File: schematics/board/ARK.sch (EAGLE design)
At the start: 85 parts, among them IC2 STM32F103C8T

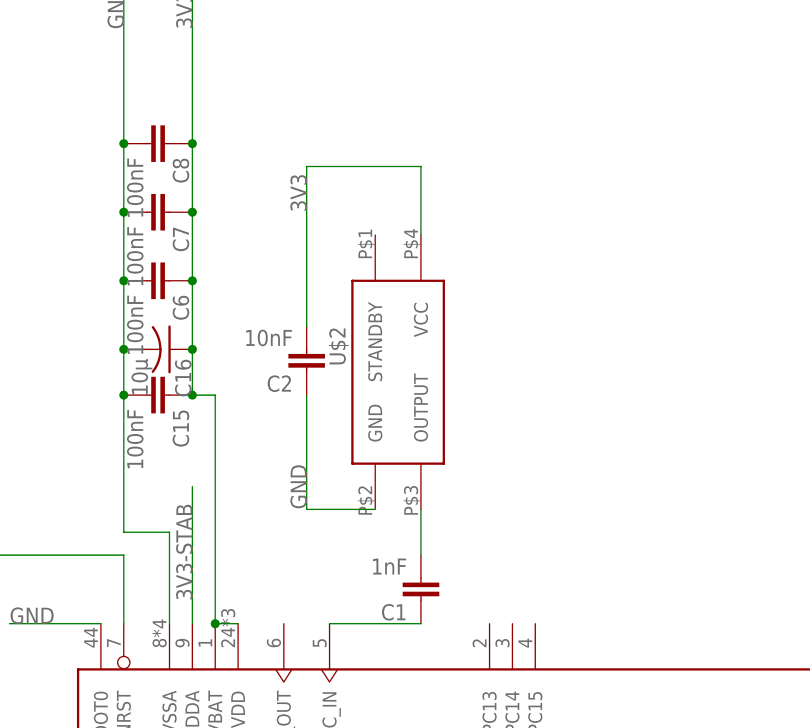
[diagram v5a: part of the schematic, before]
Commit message: Завершена разработка плат БСК5 и АРК, половина платы БКУ разведена, добавлены гербер файлы плат АРК, БСК5 и WSPR
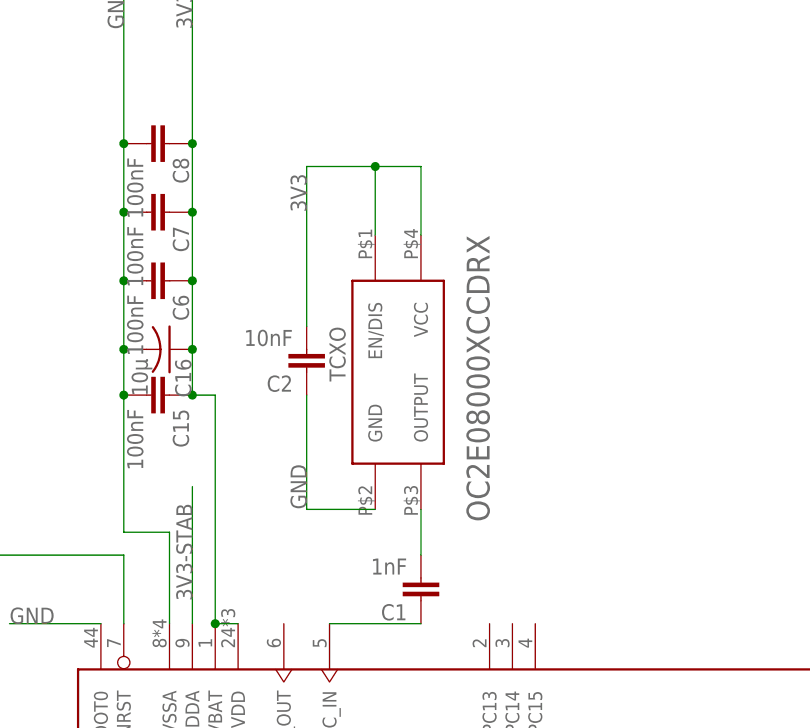
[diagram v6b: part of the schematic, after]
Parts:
- removed U$2: Q24, CanCubeSat:Q24
- added TCXO: OC2E08000XCCDRX, CanCubeSat:OC2E08000XCCDRX
- renumbered U$57 to INA219#2
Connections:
- net 3V3: now also TCXO.EN/DIS, TCXO.VCC; no longer U$2.VCC
- net GND: now also TCXO.GND; no longer U$2.GND
- net N$4: now also TCXO.OUTPUT; no longer U$2.OUTPUT
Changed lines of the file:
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@@
 <part name="R77" library="resistor" deviceset="R-US_" device="R0603" package3d_urn="urn:adsk.eagle:package:23555/3" value="10R"/>
 <part name="C10" library="rcl" library_urn="urn:adsk.eagle:library:334" deviceset="C-US" device="C0603" package3d_urn="urn:adsk.eagle:package:23616/2" value="0,1µ"/>
-<part name="U$57" library="CanCubeSat" deviceset="INA219AID" device=""/>
+<part name="INA219#2" library="CanCubeSat" deviceset="INA219AID" device=""/>
 <part name="INA219#1" library="CanCubeSat" deviceset="INA219AID" device=""/>
 <part name="U$12" library="CanCubeSat" deviceset="FFC-CONNECT" device="68611"/>
-<part name="U$2" library="CanCubeSat" deviceset="Q24" device=""/>
+<part name="TCXO" library="CanCubeSat" deviceset="OC2E08000XCCDRX" device=""/>
 <part name="C1" library="rcl" library_urn="urn:adsk.eagle:library:334" deviceset="C-EU" device="C0603" package3d_urn="urn:adsk.eagle:package:23616/2" value="1nF"/>
 <part name="C2" library="rcl" library_urn="urn:adsk.eagle:library:334" deviceset="C-EU" device="C0603" package3d_urn="urn:adsk.eagle:package:23616/2" value="10nF"/>
@@
 <attribute name="VALUE" x="-317.119" y="443.23" size="1.778" layer="96" rot="R90"/>
 </instance>
-<instance part="U$57" gate="G$1" x="-314.96" y="472.44" smashed="yes" rot="R90"/>
+<instance part="INA219#2" gate="G$1" x="-314.96" y="472.44" smashed="yes" rot="R90"/>
 <instance part="INA219#1" gate="G$1" x="-287.02" y="472.44" smashed="yes" rot="R90"/>
 <instance part="U$12" gate="G$1" x="-22.86" y="487.68" smashed="yes">
@@
 <attribute name="VALUE" x="-29.21" y="464.82" size="1.778" layer="96"/>
 </instance>
-<instance part="U$2" gate="G$1" x="160.02" y="426.72" smashed="yes" rot="R270">
+<instance part="TCXO" gate="G$1" x="160.02" y="426.72" smashed="yes" rot="R270">
 <attribute name="NAME" x="152.4" y="431.8" size="1.778" layer="95" rot="R270"/>
 </instance>
@@
 <wire x1="-285.75" y1="459.74" x2="-285.75" y2="454.66" width="0.1524" layer="91"/>
 <label x="-276.86" y="454.914" size="1.778" layer="95"/>
-<pinref part="U$57" gate="G$1" pin="GND"/>
+<pinref part="INA219#2" gate="G$1" pin="GND"/>
 <pinref part="INA219#1" gate="G$1" pin="GND"/>
 <wire x1="-285.75" y1="454.66" x2="-313.69" y2="454.66" width="0.1524" layer="91"/>
@@
 <junction x="-290.83" y="487.68"/>
 <label x="-276.86" y="487.68" size="1.778" layer="95"/>
-<pinref part="U$57" gate="G$1" pin="A1"/>
+<pinref part="INA219#2" gate="G$1" pin="A1"/>
 <pinref part="INA219#1" gate="G$1" pin="A1"/>
 <pinref part="INA219#1" gate="G$1" pin="A0"/>
@@
 <wire x1="149.86" y1="411.48" x2="157.48" y2="411.48" width="0.1524" layer="91"/>
 <label x="149.86" y="411.48" size="1.778" layer="95" rot="R90"/>
-<pinref part="U$2" gate="G$1" pin="GND"/>
+<pinref part="TCXO" gate="G$1" pin="GND"/>
 <pinref part="C2" gate="G$1" pin="1"/>
 </segment>
@@
 <wire x1="-283.21" y1="485.14" x2="-283.21" y2="490.22" width="0.1524" layer="91"/>
 <label x="-276.86" y="490.22" size="1.778" layer="95"/>
-<pinref part="U$57" gate="G$1" pin="SCL"/>
+<pinref part="INA219#2" gate="G$1" pin="SCL"/>
 <pinref part="INA219#1" gate="G$1" pin="SCL"/>
 <wire x1="-283.21" y1="490.22" x2="-311.15" y2="490.22" width="0.1524" layer="91"/>
@@
 <wire x1="-285.75" y1="485.14" x2="-285.75" y2="492.76" width="0.1524" layer="91"/>
 <label x="-276.86" y="492.76" size="1.778" layer="95"/>
-<pinref part="U$57" gate="G$1" pin="SDA"/>
+<pinref part="INA219#2" gate="G$1" pin="SDA"/>
 <pinref part="INA219#1" gate="G$1" pin="SDA"/>
 <wire x1="-285.75" y1="492.76" x2="-313.69" y2="492.76" width="0.1524" layer="91"/>
@@
 <pinref part="R76" gate="G$1" pin="2"/>
 <pinref part="C10" gate="G$1" pin="1"/>
-<pinref part="U$57" gate="G$1" pin="IN+"/>
+<pinref part="INA219#2" gate="G$1" pin="IN+"/>
 <wire x1="-326.39" y1="450.088" x2="-326.39" y2="439.674" width="0.1524" layer="91"/>
 <wire x1="-318.77" y1="459.74" x2="-318.77" y2="450.088" width="0.1524" layer="91"/>
@@
 <pinref part="R77" gate="G$1" pin="2"/>
 <pinref part="C10" gate="G$1" pin="2"/>
-<pinref part="U$57" gate="G$1" pin="IN-"/>
+<pinref part="INA219#2" gate="G$1" pin="IN-"/>
 </segment>
 </net>
@@
 <junction x="-311.15" y="457.2"/>
 <label x="-276.86" y="457.2" size="1.778" layer="95"/>
-<pinref part="U$57" gate="G$1" pin="A0"/>
-<pinref part="U$57" gate="G$1" pin="VS"/>
+<pinref part="INA219#2" gate="G$1" pin="A0"/>
+<pinref part="INA219#2" gate="G$1" pin="VS"/>
 <pinref part="INA219#1" gate="G$1" pin="VS"/>
 <wire x1="-283.21" y1="457.2" x2="-271.78" y2="457.2" width="0.1524" layer="91"/>
@@
 <segment>
 <wire x1="162.56" y1="441.96" x2="162.56" y2="449.58" width="0.1524" layer="91"/>
-<wire x1="162.56" y1="449.58" x2="149.86" y2="449.58" width="0.1524" layer="91"/>
+<wire x1="162.56" y1="449.58" x2="157.48" y2="449.58" width="0.1524" layer="91"/>
+<wire x1="157.48" y1="449.58" x2="149.86" y2="449.58" width="0.1524" layer="91"/>
 <wire x1="149.86" y1="449.58" x2="149.86" y2="431.8" width="0.1524" layer="91"/>
 <label x="149.86" y="444.5" size="1.778" layer="95" rot="R90"/>
-<pinref part="U$2" gate="G$1" pin="VCC"/>
+<pinref part="TCXO" gate="G$1" pin="VCC"/>
 <pinref part="C2" gate="G$1" pin="2"/>
+<pinref part="TCXO" gate="G$1" pin="EN/DIS"/>
+<wire x1="157.48" y1="441.96" x2="157.48" y2="449.58" width="0.1524" layer="91"/>
+<junction x="157.48" y="449.58"/>
 </segment>
 <segment>
@@
 <segment>
 <wire x1="162.56" y1="406.4" x2="162.56" y2="411.48" width="0.1524" layer="91"/>
-<pinref part="U$2" gate="G$1" pin="OUTPUT"/>
+<pinref part="TCXO" gate="G$1" pin="OUTPUT"/>
 <pinref part="C1" gate="G$1" pin="2"/>
 </segment>
